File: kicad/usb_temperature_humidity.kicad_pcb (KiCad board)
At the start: 2 copper layers, 72 x 47.5 mm, 15 parts, among them SW1 SW_SPDT, SW2 SW_SPDT, U1 SeeeduinoXIAO, U2 SHT-31, U3 PinHeader_XIAO, U4 PinHeader_XIAO, U5 SHT-31_aliexpress

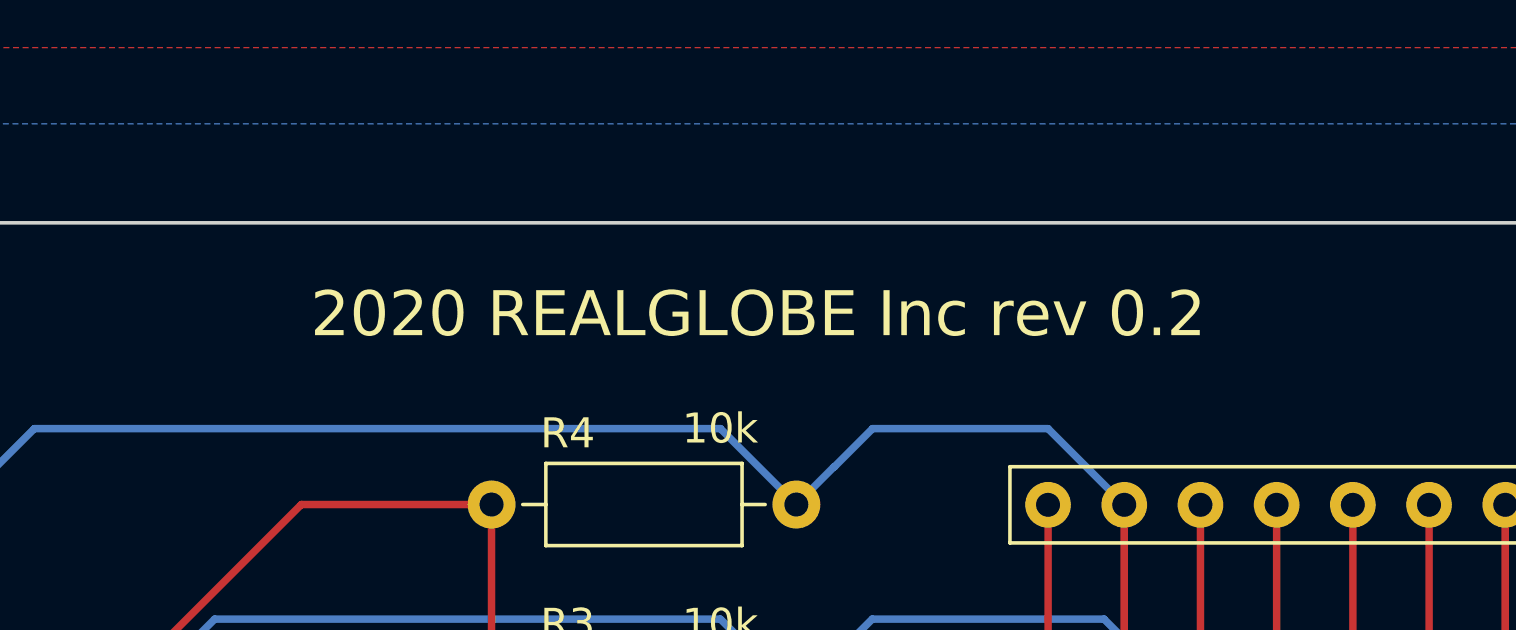
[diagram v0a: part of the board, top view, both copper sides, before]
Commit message: バージョンシルクのインクリメントをした
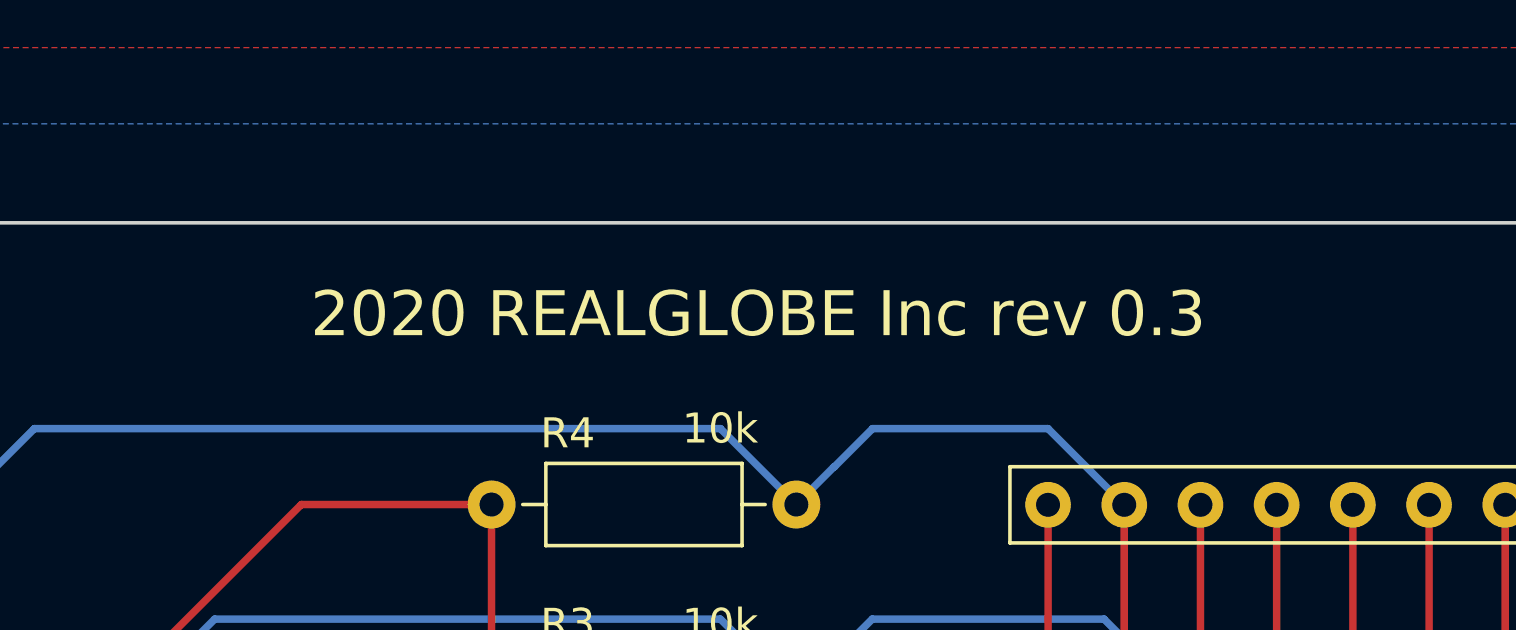
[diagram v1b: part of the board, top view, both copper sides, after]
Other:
- board text added: "2020 REALGLOBE Inc rev 0.3"
- board text removed: "2020 REALGLOBE Inc rev 0.2"
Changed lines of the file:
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@@
     (effects (font (size 1 1) (thickness 0.15)))
   )
-  (gr_text "2020 REALGLOBE Inc rev 0.2" (at 34.29 -44.45) (layer F.SilkS)
+  (gr_text "2020 REALGLOBE Inc rev 0.3" (at 34.29 -44.45) (layer F.SilkS)
     (effects (font (size 1.5 1.5) (thickness 0.3)))
   )
